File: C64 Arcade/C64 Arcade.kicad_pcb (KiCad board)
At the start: 2 copper layers, 99.7 x 55.2 mm, 48 parts, among them J1 Port_1, J10 P2_FIRE3, J11 P1_FIRE1, J12 P1_FIRE2, J13 P1_FIRE3, J14 EXT_PWR, J15 DIR_LEFT, J2 Port_2, J3 DIR_RIGHT, J4 UP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

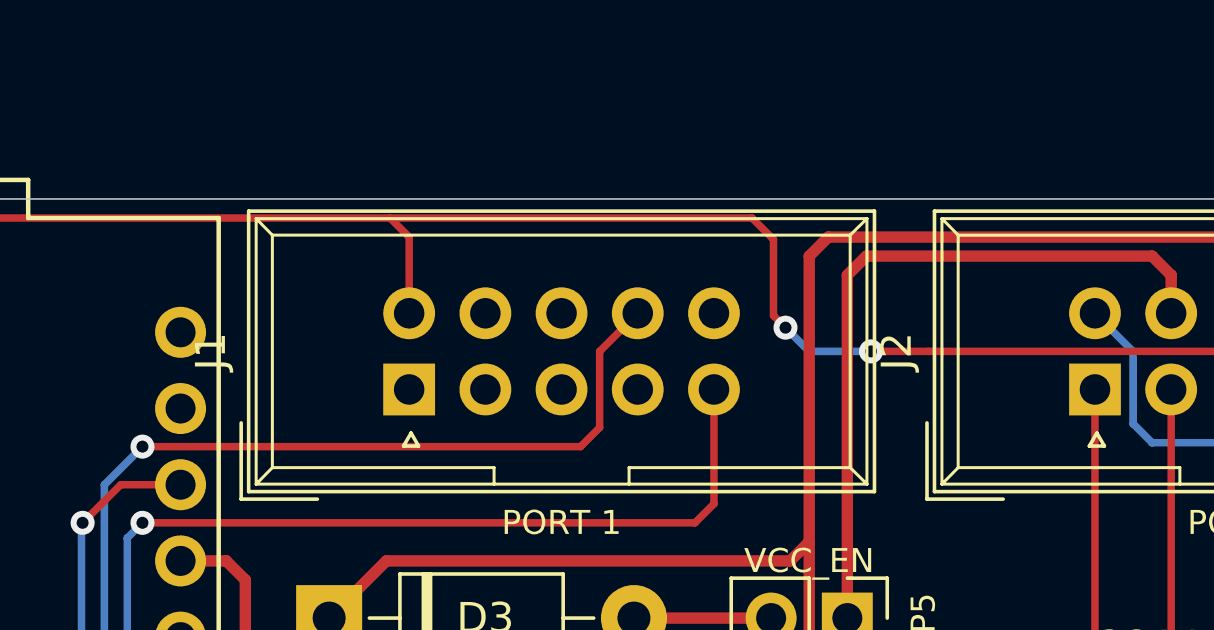
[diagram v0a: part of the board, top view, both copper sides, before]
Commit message: Tweaked faceplates to allow more leeway on LEDs
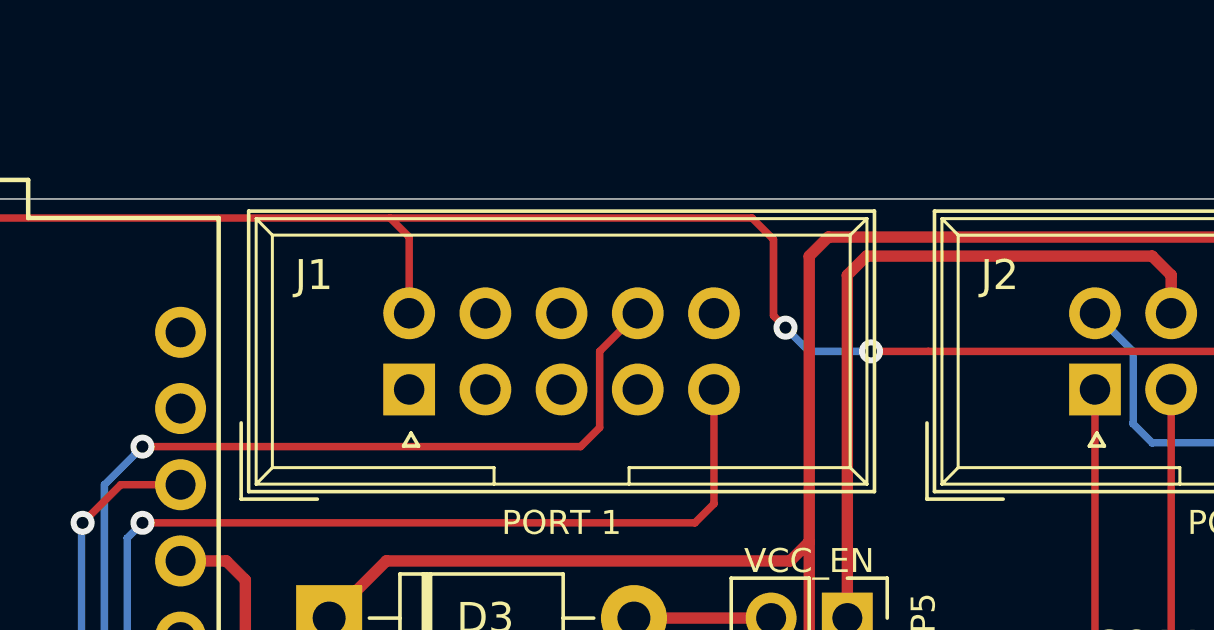
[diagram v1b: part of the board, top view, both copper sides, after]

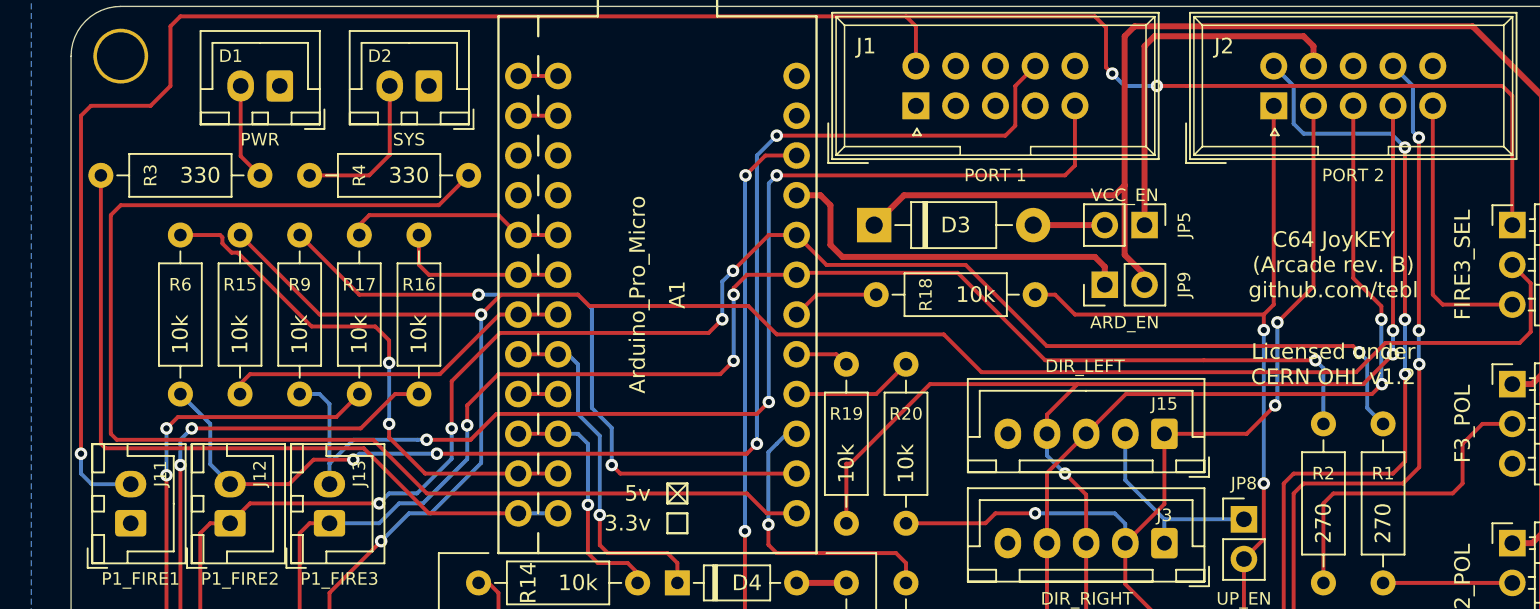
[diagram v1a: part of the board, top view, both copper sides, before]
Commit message: Add one more button to arcade board
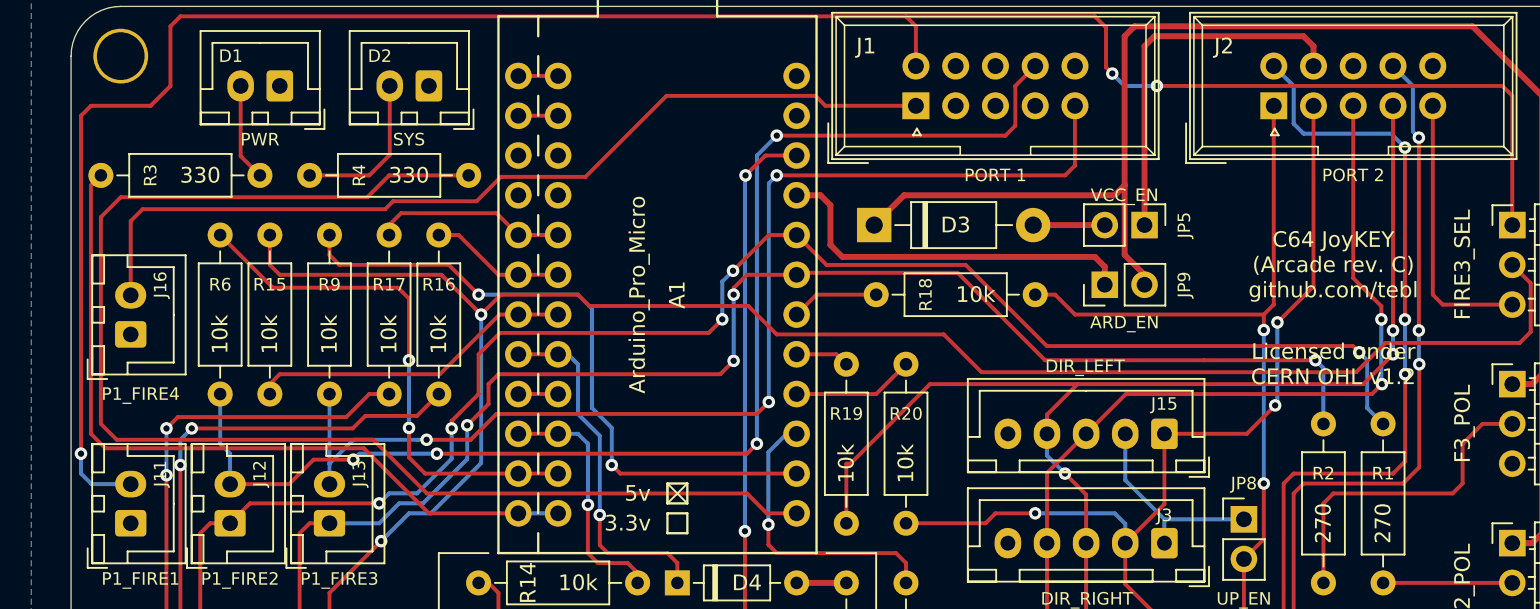
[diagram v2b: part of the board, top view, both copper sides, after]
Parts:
- added J16: P1_FIRE4, Connector_JST:JST_XH_B2B-XH-A_1x02_P2.50mm_Vertical, F.Cu at (144.8, 103.5)
- moved R6 2.54 mm to (150.5, 97.2)
- moved R15 1.91 mm to (153.7, 107.3)
- moved R17 1.91 mm to (161.3, 97.2)
- moved R9 1.91 mm to (157.5, 107.3)
- moved R16 1.27 mm to (164.5, 97.2)
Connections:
- J1 pad 1: (no net) -> P1_FIRE4
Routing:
- net P1_FIRE4: track 0.00 -> 58.5 mm
- net /FIRE2_IN: track 11.1 -> 8.67 mm
- net P1_FIRE3: track 74.8 -> 72.6 mm
- net Net-(J8-Pad2): track 79.1 -> 81.0 mm
- net /FIRE3_IN: track 22.8 -> 20.9 mm
- net /FIRE1_IN: track 14.1 -> 12.3 mm
- net Net-(J9-Pad2): track 79.7 -> 80.9 mm
- net Net-(A1-Pad14): track 43.2 -> 42.0 mm
- net P1_FIRE2: track 81.8 -> 80.8 mm
- net /SYS: track 83.8 -> 84.6 mm
- net Net-(J10-Pad2): track 121.3 -> 120.6 mm
- net /PWR: track 48.2 -> 48.7 mm
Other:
- board text added: "C64 JoyKEY (Arcade rev. C) github.com/tebl"
- board text added: "P1_FIRE4"
- board text removed: "C64 JoyKEY (Arcade rev. B) github.com/tebl"
